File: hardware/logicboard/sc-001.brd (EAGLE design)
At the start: 92 x 58 mm, 10 parts

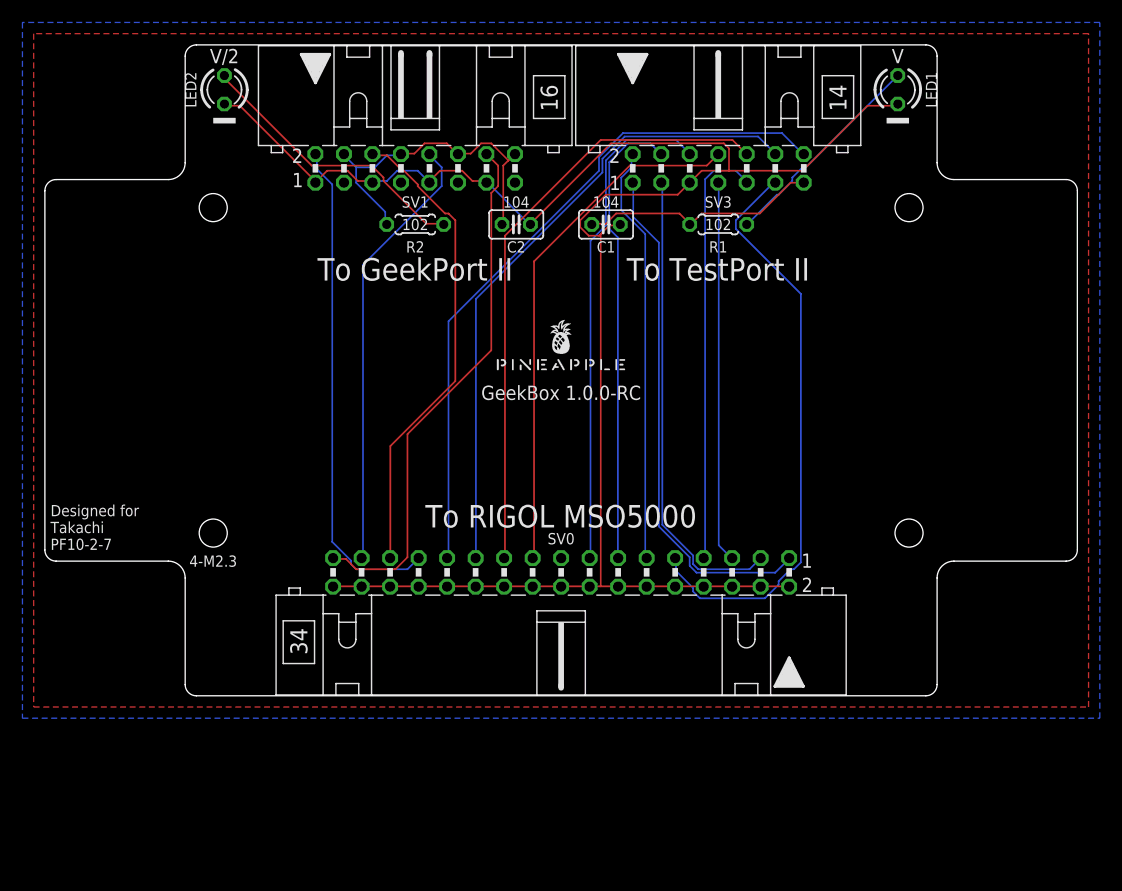
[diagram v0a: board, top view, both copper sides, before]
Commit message: Changed board size.
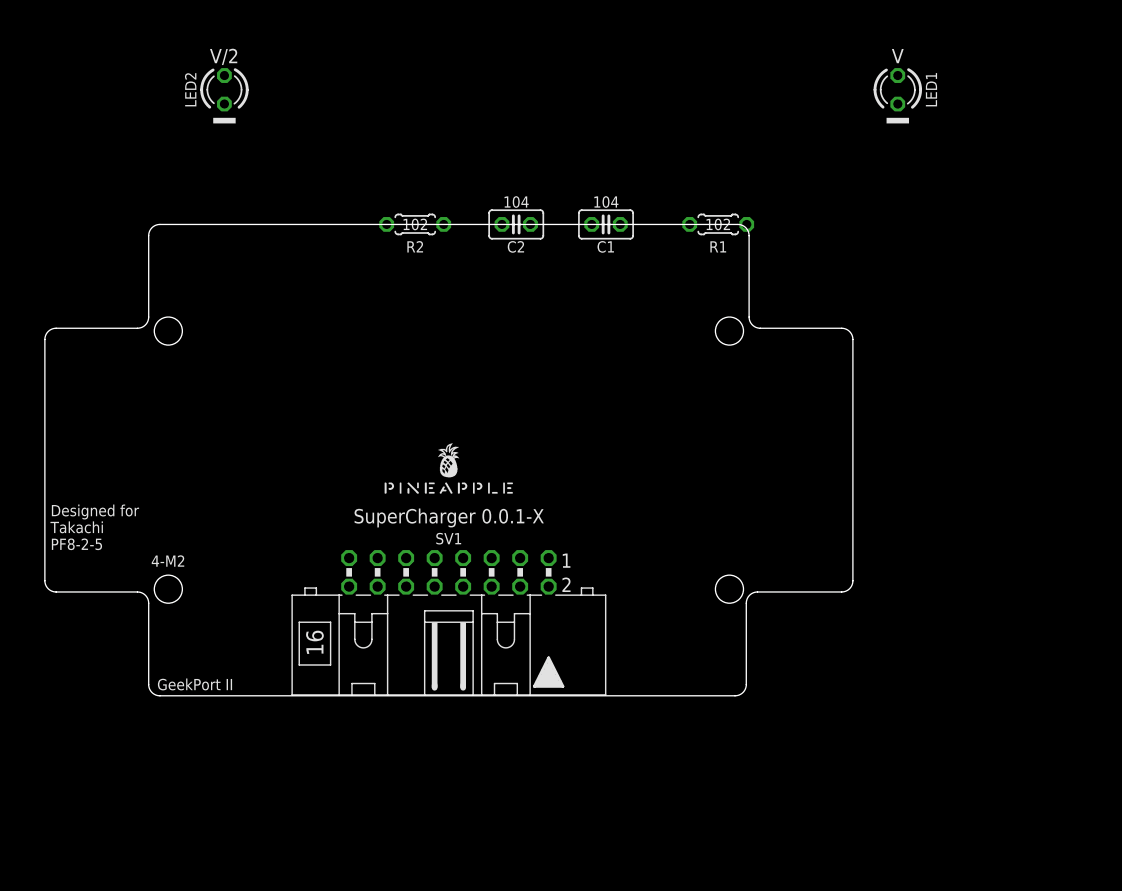
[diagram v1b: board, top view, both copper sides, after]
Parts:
- removed SV0: (no value), con-ml:ML34L
- removed SV3: (no value), con-ml:ML14L
- moved SV1 36.1 mm to (36.0, 11.0), turned to 180 degrees
- moved U$1 14.9 mm to (36.0, 18.0)
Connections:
- removed net GB00: SV0.1, SV3.1
- removed net GB01: SV0.3, SV3.3
- removed net GB02: SV0.5, SV3.7
- removed net GB03: SV0.7, SV3.9
- removed net GB04: SV0.9, SV3.11
- removed net GB05: SV0.11, SV3.2
- removed net GB06: SV0.13, SV3.4
- removed net GB07: SV0.15, SV3.6
- removed net GB08: SV0.19, SV3.8
- removed net GB09: SV0.21, SV3.10
- removed net GB10: SV0.23, SV3.12
- removed net GB11: SV0.25, SV3.14
- net GB12: no longer SV0.27
- net GB13: no longer SV0.29
- net GB14: no longer SV0.31
- net GB15: no longer SV0.33
- net GND: no longer SV0.10, SV0.12, SV0.14, SV0.16, SV0.18, SV0.2, SV0.20, SV0.22, SV0.24, SV0.26, SV0.28, SV0.30, SV0.32, SV0.34, SV0.4, SV0.6, SV0.8, SV3.5
- net VCC: no longer SV3.13
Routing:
- net GND: track 167.3 -> 0.00 mm
- net GB11: track 61.3 -> 0.00 mm
- net GB10: track 57.1 -> 0.00 mm
- net GB09: track 54.4 -> 0.00 mm
- net GB04: track 53.0 -> 0.00 mm
- net GB15: track 47.2 -> 0.00 mm
- net GB08: track 46.9 -> 0.00 mm
- net GB00: track 45.9 -> 0.00 mm
- net GB07: track 44.8 -> 0.00 mm
- net GB12: track 44.5 -> 0.00 mm
- net GB13: track 42.4 -> 0.00 mm
- net GB01: track 41.8 -> 0.00 mm
- net GB06: track 41.3 -> 0.00 mm
- net GB14: track 39.4 -> 0.00 mm
- net GB03: track 38.3 -> 0.00 mm
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- removed copper zone on layer 1, net GND
- removed copper zone on layer 16, net GND
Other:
- board size 92 x 58 mm -> 72 x 42 mm
- board text added: "4-M2"
- board text added: "Designed for Takachi PF8-2-5"
- board text added: "GeekPort II"
- board text added: "SuperCharger 0.0.1-X"
- board text removed: "4-M2.3"
- board text removed: "Designed for Takachi PF10-2-7"
- board text removed: "GeekBox 1.0.0-RC"
- board text removed: "To GeekPort II"
- board text removed: "To RIGOL MSO5000"
- board text removed: "To TestPort II"

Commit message: Added parts.
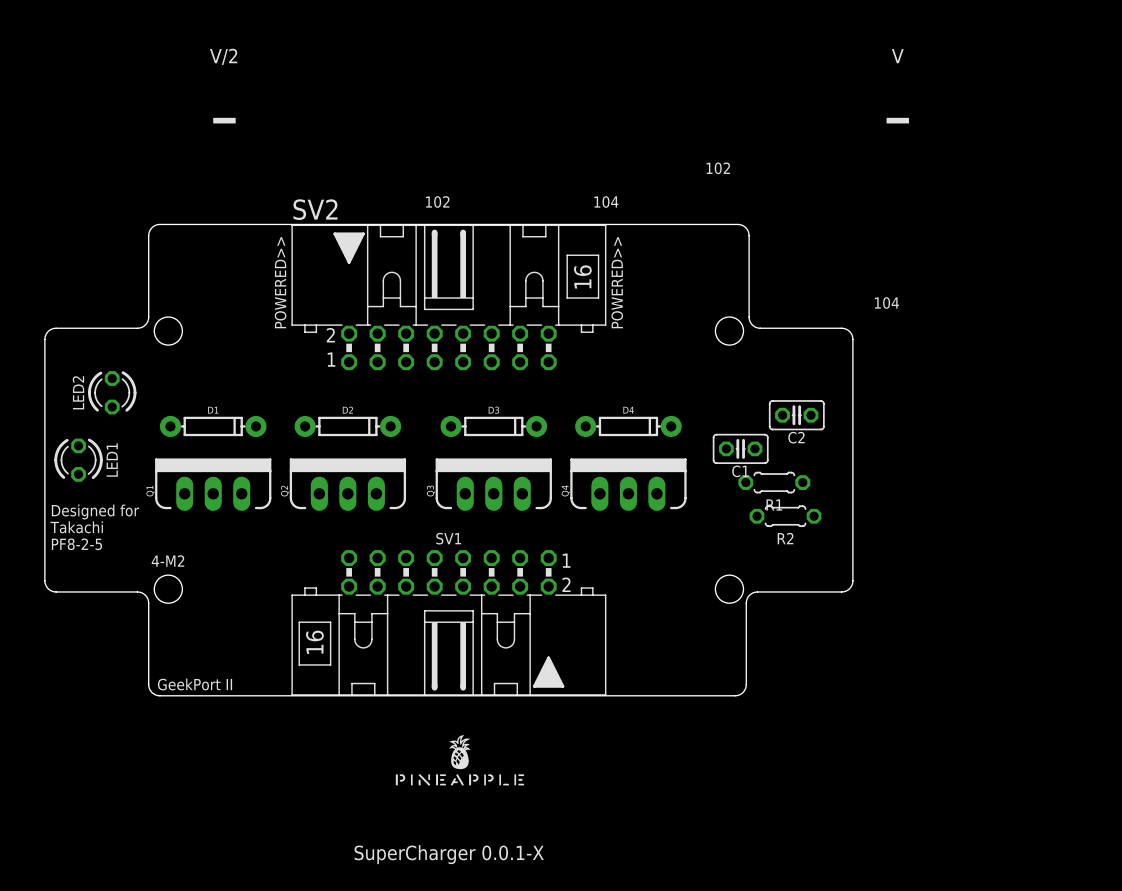
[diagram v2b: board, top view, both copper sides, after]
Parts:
- added D1, D2, D3, D4: 200mA/100V/1V, SparkFun-DiscreteSemi:DIODE-1N4148
- added Q1, Q2, Q3, Q4: 60V/32A/35mΩ, SparkFun-DiscreteSemi:TO220V
- added SV2: (no value), con-ml:ML16L
- moved LED1 80.1 mm to (3.00, 21.0)
- moved R2 42.0 mm to (66.0, 16.0)
- moved C2 30.2 mm to (67.0, 25.0)
- moved LED2 28.8 mm to (6.00, 27.0)
- moved U$1 26.0 mm to (37.0, -8.00)
- moved R1 23.5 mm to (65.0, 19.0)
- moved C1 23.3 mm to (62.0, 22.0)
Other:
- board text added: "POWERED>>"

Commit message: Schematic.
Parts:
- moved LED1 22.7 mm to (18.0, 4.00)
- moved LED2 16.3 mm to (18.0, 38.0)
- moved Q1 4.24 mm to (18.0, 21.0)
- moved Q2 4.24 mm to (30.0, 21.0)
- moved D1 3.61 mm to (18.0, 26.0)
- moved D2 3.61 mm to (30.0, 26.0)
- moved Q3 3.61 mm to (42.0, 21.0)
- moved Q4 3.61 mm to (54.0, 21.0)
- moved D3 2.83 mm to (42.0, 26.0)
- moved D4 2.83 mm to (54.0, 26.0)
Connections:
- removed net GB12: SV1.2
- removed net GB13: SV1.6
- removed net GB14: SV1.10
- removed net GB15: SV1.14
- new net ANLG0: SV1.3
- new net ANLG1: SV1.7
- new net ANLG2: SV1.11
- new net ANLG3: SV1.15
- new net DRVR0: D1.A, Q1.2
- new net DRVR1: D2.A, Q2.2
- new net DRVR2: D3.A, Q3.2
- new net DRVR3: D4.A, Q4.2
- new net DTCT0: Q1.1, SV1.2
- new net DTCT1: Q2.1, SV1.6
- new net DTCT2: Q3.1, SV1.10
- new net DTCT3: Q4.1, SV1.14
- net GND: now also Q1.3, Q2.3, Q3.3, Q4.3
- net VCC/2: now also D1.C, D2.C, D3.C, D4.C

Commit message: Routed.
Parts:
- removed C2: (no value), rcl:C025-025X050
- removed LED2: (no value), led:LED3MM
- removed R2: 1k, rcl:0204/5
- moved R1 48.3 mm to (18.0, 30.0)
- moved C1 47.5 mm to (18.0, 4.00)
- moved U$1 42.4 mm to (68.0, 21.0), turned to 90 degrees
- moved LED1 34.0 mm to (18.0, 38.0)
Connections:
- removed net VCC: C1.1, R1.1
- removed net VCCLED: LED1.A, R1.2
- net ANLG0: now also SV2.3
- net ANLG1: now also SV2.7
- net ANLG2: now also SV2.11
- net ANLG3: now also SV2.15
- net DRVR0: now also SV2.2
- net DRVR1: now also SV2.6
- net DRVR2: now also SV2.10
- net DRVR3: now also SV2.14
- net GND: now also SV2.1, SV2.13, SV2.5, SV2.9; no longer C2.2, LED2.K
- net VCC/2: now also C1.1, R1.1, SV2.12, SV2.16, SV2.4, SV2.8; no longer C2.1, R2.1
- net VCC2LED: now also LED1.A, R1.2; no longer LED2.A, R2.2
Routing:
- net GND: track 0.00 -> 114.4 mm
- net VCC/2: track 0.00 -> 113.0 mm
- net DTCT0: track 0.00 -> 36.1 mm
- net ANLG3: track 0.00 -> 35.0 mm
- net ANLG0: track 0.00 -> 32.8 mm, vias 0 -> 1
- net DTCT3: track 0.00 -> 27.8 mm
- net ANLG2: track 0.00 -> 24.2 mm
- net ANLG1: track 0.00 -> 21.4 mm
- net DRVR0: track 0.00 -> 20.6 mm
- net DTCT1: track 0.00 -> 20.1 mm
- net DRVR3: track 0.00 -> 17.1 mm
- net DRVR1: track 0.00 -> 15.6 mm
- net DRVR2: track 0.00 -> 13.4 mm
- net DTCT2: track 0.00 -> 13.2 mm
- net VCC2LED: track 0.00 -> 10.3 mm
- added copper zone on layer 1, net GND
- added copper zone on layer 16, net GND
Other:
- board text removed: "V"
- board text removed: "V/2"
